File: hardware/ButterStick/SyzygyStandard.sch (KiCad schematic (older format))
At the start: 9 parts, among them J1 SYZYGY-STD, U2 DAC081C081CIMK, U7 TPS73101DBV

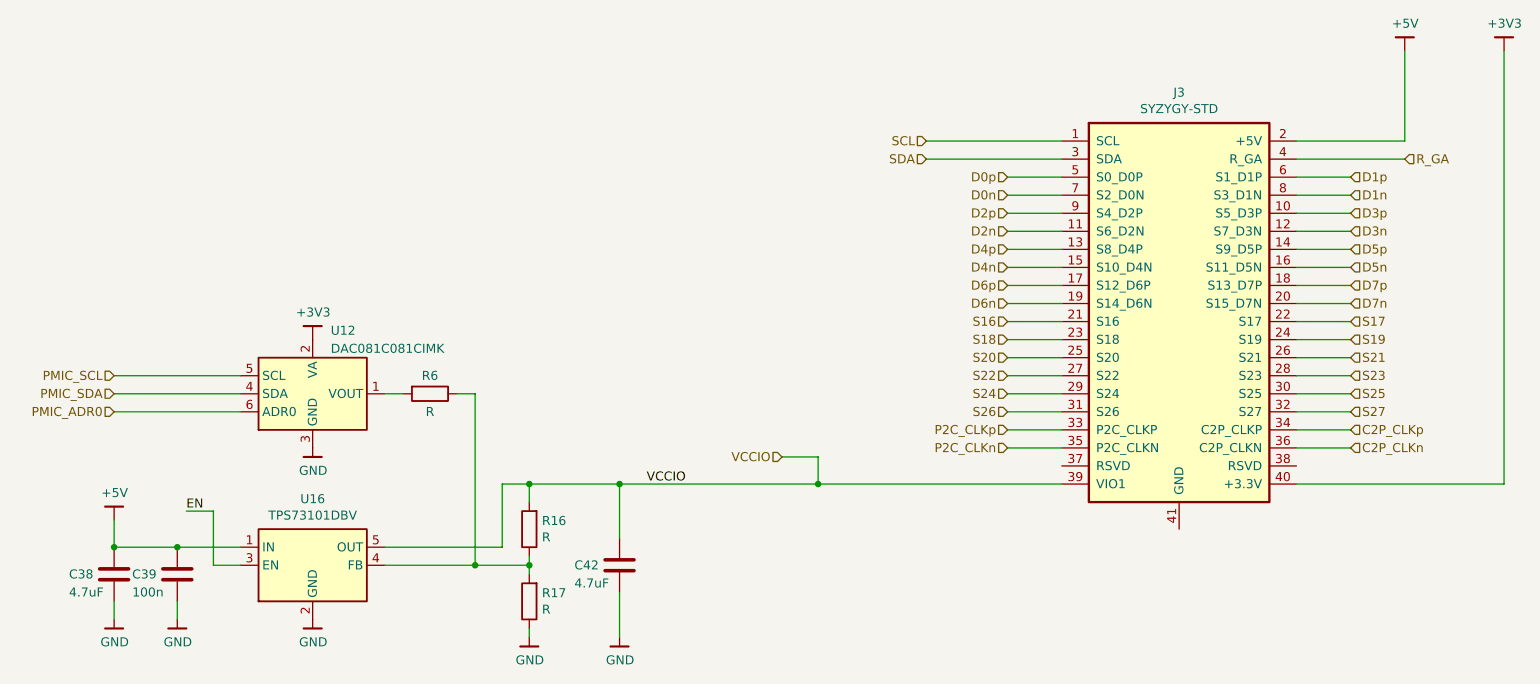
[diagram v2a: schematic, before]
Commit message: Added ESD on SD card signals.
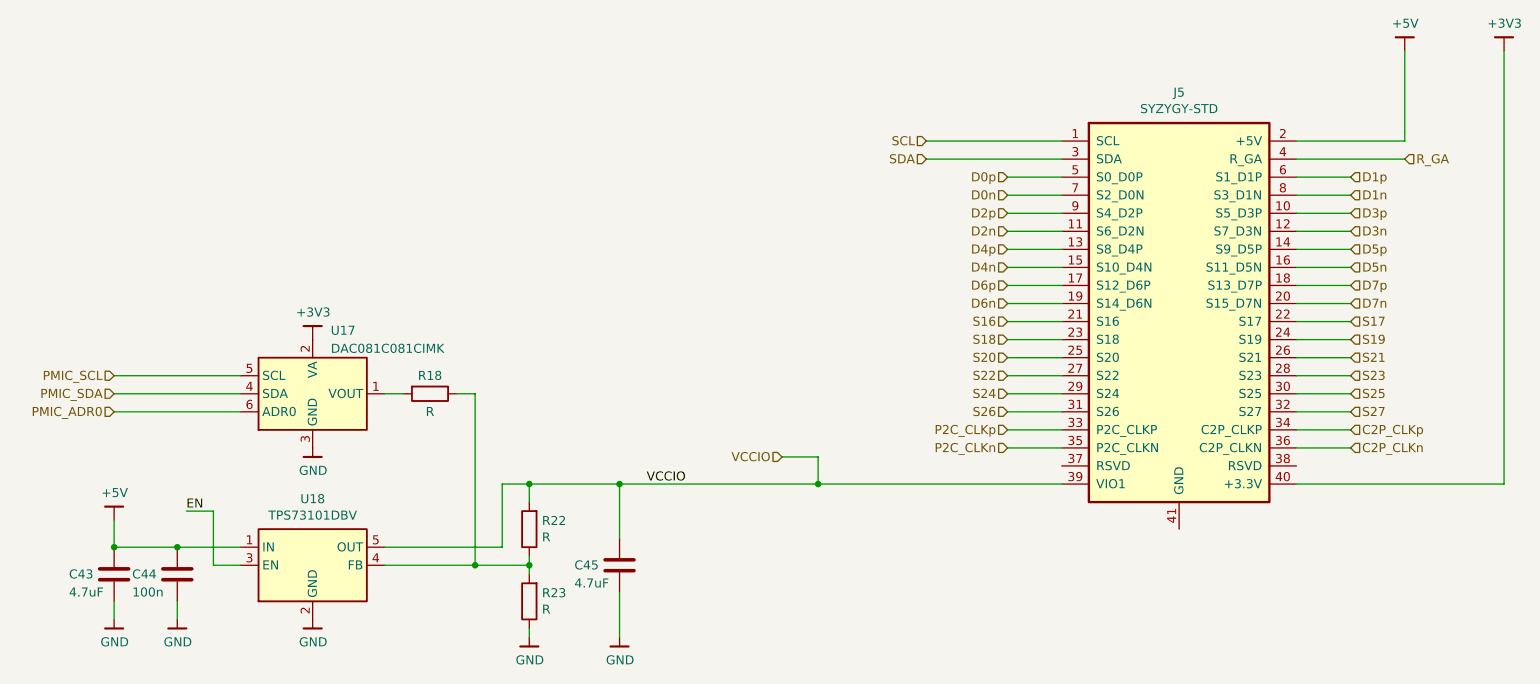
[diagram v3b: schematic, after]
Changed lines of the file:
@@
 $Descr A4 11693 8268
 encoding utf-8
-Sheet 13 14
+Sheet 9 13
 Title ""
 Date ""
@@
 AR Path="/5C80F19D/5C8A3B67/5C813052" Ref="J3"  Part="1"
 AR Path="/5C80F1A0/5C8EBB21/5C813052" Ref="J5"  Part="1"
-F 0 "J3" H 7850 4819 50  0000 C CNN
+F 0 "J5" H 7850 4819 50  0000 C CNN
 F 1 "SYZYGY-STD" H 7850 4728 50  0000 C CNN
 F 2 "gkl_conn:SYZYGY_standard_carrier" H 7850 4700 50  0001 C CNN
@@
 AR Path="/5C80F19D/5C8A3B67/5C939EEE" Ref="U16"  Part="1"
 AR Path="/5C80F1A0/5C8EBB21/5C939EEE" Ref="U18"  Part="1"
-F 0 "U16" H 3050 5567 50  0000 C CNN
+F 0 "U18" H 3050 5567 50  0000 C CNN
 F 1 "TPS73101DBV" H 3050 5476 50  0000 C CNN
 F 2 "Package_TO_SOT_SMD:SOT-23-5" H 3050 5525 50  0001 C CIN
@@
 AR Path="/5C80F19D/5C8A3B67/5C939EF5" Ref="U12"  Part="1"
 AR Path="/5C80F1A0/5C8EBB21/5C939EF5" Ref="U17"  Part="1"
-F 0 "U12" H 3150 4600 50  0000 L CNN
+F 0 "U17" H 3150 4600 50  0000 L CNN
 F 1 "DAC081C081CIMK" H 3150 4500 50  0000 L CNN
 F 2 "Package_TO_SOT_SMD:SOT-23-6" H 3700 4000 50  0001 C CNN
@@
 AR Path="/5C80F19D/5C8A3B67/5C9A2E64" Ref="#PWR0140"  Part="1"
 AR Path="/5C80F1A0/5C8EBB21/5C9A2E64" Ref="#PWR0183"  Part="1"
-F 0 "#PWR0140" H 3050 4300 50  0001 C CNN
+F 0 "#PWR0183" H 3050 4300 50  0001 C CNN
 F 1 "GND" H 3053 4424 50  0000 C CNN
 F 2 "" H 2950 4200 50  0001 C CNN
@@
 AR Path="/5C80F19D/5C8A3B67/5C939F02" Ref="#PWR0173"  Part="1"
 AR Path="/5C80F1A0/5C8EBB21/5C939F02" Ref="#PWR0184"  Part="1"
-F 0 "#PWR0173" H 3050 5250 50  0001 C CNN
+F 0 "#PWR0184" H 3050 5250 50  0001 C CNN
 F 1 "GND" H 3053 5374 50  0000 C CNN
 F 2 "" H 2950 5150 50  0001 C CNN
@@
 AR Path="/5C80F19D/5C8A3B67/5C9A2E66" Ref="#PWR0174"  Part="1"
 AR Path="/5C80F1A0/5C8EBB21/5C9A2E66" Ref="#PWR0185"  Part="1"
-F 0 "#PWR0174" H 3050 3800 50  0001 C CNN
+F 0 "#PWR0185" H 3050 3800 50  0001 C CNN
 F 1 "+3V3" H 3053 4101 50  0000 C CNN
 F 2 "" H 3050 3950 50  0001 C CNN
@@
 AR Path="/5C80F19D/5C8A3B67/5C939F0E" Ref="#PWR0175"  Part="1"
 AR Path="/5C80F1A0/5C8EBB21/5C939F0E" Ref="#PWR0186"  Part="1"
-F 0 "#PWR0175" H 1950 4800 50  0001 C CNN
+F 0 "#PWR0186" H 1950 4800 50  0001 C CNN
 F 1 "+5V" H 1953 5101 50  0000 C CNN
 F 2 "" H 1950 4950 50  0001 C CNN
@@
 AR Path="/5C80F19D/5C8A3B67/5C9A2E68" Ref="C38"  Part="1"
 AR Path="/5C80F1A0/5C8EBB21/5C9A2E68" Ref="C43"  Part="1"
-F 0 "C38" H 1700 5250 50  0000 L CNN
+F 0 "C43" H 1700 5250 50  0000 L CNN
 F 1 "4.7uF" H 1700 5150 50  0000 L CNN
 F 2 "pkl_dipol:C_0603" H 1988 5100 50  0001 C CNN
@@
 AR Path="/5C80F19D/5C8A3B67/5C939F1D" Ref="C39"  Part="1"
 AR Path="/5C80F1A0/5C8EBB21/5C939F1D" Ref="C44"  Part="1"
-F 0 "C39" H 2050 5250 50  0000 L CNN
+F 0 "C44" H 2050 5250 50  0000 L CNN
 F 1 "100n" H 2050 5150 50  0000 L CNN
 F 2 "pkl_dipol:C_0402" H 2338 5100 50  0001 C CNN
@@
 AR Path="/5C80F19D/5C8A3B67/5C9A2E6A" Ref="R6"  Part="1"
 AR Path="/5C80F1A0/5C8EBB21/5C9A2E6A" Ref="R18"  Part="1"
-F 0 "R6" V 3600 4250 50  0000 C CNN
+F 0 "R18" V 3600 4250 50  0000 C CNN
 F 1 "R" V 3800 4250 50  0000 C CNN
 F 2 "pkl_dipol:C_0402" V 3630 4250 50  0001 C CNN
@@
 AR Path="/5C80F19D/5C8A3B67/5C939F38" Ref="R16"  Part="1"
 AR Path="/5C80F1A0/5C8EBB21/5C939F38" Ref="R22"  Part="1"
-F 0 "R16" H 4180 4954 50  0000 R CNN
+F 0 "R22" H 4180 4954 50  0000 R CNN
 F 1 "R" H 4180 5045 50  0000 R CNN
 F 2 "pkl_dipol:C_0402" V 4180 5000 50  0001 C CNN
@@
 AR Path="/5C80F19D/5C8A3B67/5C939F3F" Ref="R17"  Part="1"
 AR Path="/5C80F1A0/5C8EBB21/5C939F3F" Ref="R23"  Part="1"
-F 0 "R17" H 4180 5354 50  0000 R CNN
+F 0 "R23" H 4180 5354 50  0000 R CNN
 F 1 "R" H 4180 5445 50  0000 R CNN
 F 2 "pkl_dipol:C_0402" V 4180 5400 50  0001 C CNN
@@
 AR Path="/5C80F19D/5C8A3B67/5C939F46" Ref="C42"  Part="1"
 AR Path="/5C80F1A0/5C8EBB21/5C939F46" Ref="C45"  Part="1"
-F 0 "C42" H 4500 5200 50  0000 L CNN
+F 0 "C45" H 4500 5200 50  0000 L CNN
 F 1 "4.7uF" H 4500 5100 50  0000 L CNN
 F 2 "pkl_dipol:C_0603" H 4788 5050 50  0001 C CNN
@@
 AR Path="/5C80F19D/5C8A3B67/5C939F4E" Ref="#PWR0176"  Part="1"
 AR Path="/5C80F1A0/5C8EBB21/5C939F4E" Ref="#PWR0187"  Part="1"
-F 0 "#PWR0176" H 4250 5350 50  0001 C CNN
+F 0 "#PWR0187" H 4250 5350 50  0001 C CNN
 F 1 "GND" H 4253 5474 50  0000 C CNN
 F 2 "" H 4150 5250 50  0001 C CNN
@@
 AR Path="/5C80F19D/5C8A3B67/5C9A2E6F" Ref="#PWR0177"  Part="1"
 AR Path="/5C80F1A0/5C8EBB21/5C9A2E6F" Ref="#PWR0188"  Part="1"
-F 0 "#PWR0177" H 4750 5350 50  0001 C CNN
+F 0 "#PWR0188" H 4750 5350 50  0001 C CNN
 F 1 "GND" H 4753 5474 50  0000 C CNN
 F 2 "" H 4650 5250 50  0001 C CNN
@@
 AR Path="/5C80F19D/5C8A3B67/5C939F6F" Ref="#PWR0178"  Part="1"
 AR Path="/5C80F1A0/5C8EBB21/5C939F6F" Ref="#PWR0189"  Part="1"
-F 0 "#PWR0178" H 2300 5250 50  0001 C CNN
+F 0 "#PWR0189" H 2300 5250 50  0001 C CNN
 F 1 "GND" H 2303 5374 50  0000 C CNN
 F 2 "" H 2200 5150 50  0001 C CNN
@@
 AR Path="/5C80F19D/5C8A3B67/5C939F75" Ref="#PWR0179"  Part="1"
 AR Path="/5C80F1A0/5C8EBB21/5C939F75" Ref="#PWR0190"  Part="1"
-F 0 "#PWR0179" H 1950 5250 50  0001 C CNN
+F 0 "#PWR0190" H 1950 5250 50  0001 C CNN
 F 1 "GND" H 1953 5374 50  0000 C CNN
 F 2 "" H 1850 5150 50  0001 C CNN
@@
 AR Path="/5C80F19D/5C8A3B67/5C946418" Ref="#PWR0181"  Part="1"
 AR Path="/5C80F1A0/5C8EBB21/5C946418" Ref="#PWR0191"  Part="1"
-F 0 "#PWR0181" H 9100 2200 50  0001 C CNN
+F 0 "#PWR0191" H 9100 2200 50  0001 C CNN
 F 1 "+5V" H 9103 2501 50  0000 C CNN
 F 2 "" H 9100 2350 50  0001 C CNN
@@
 AR Path="/5C80F19D/5C8A3B67/5C946494" Ref="#PWR0182"  Part="1"
 AR Path="/5C80F1A0/5C8EBB21/5C946494" Ref="#PWR0211"  Part="1"
-F 0 "#PWR0182" H 9650 2200 50  0001 C CNN
+F 0 "#PWR0211" H 9650 2200 50  0001 C CNN
 F 1 "+3V3" H 9653 2501 50  0000 C CNN
 F 2 "" H 9650 2350 50  0001 C CNN

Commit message: Finished initial routing of PCB.. Most parts are finished.
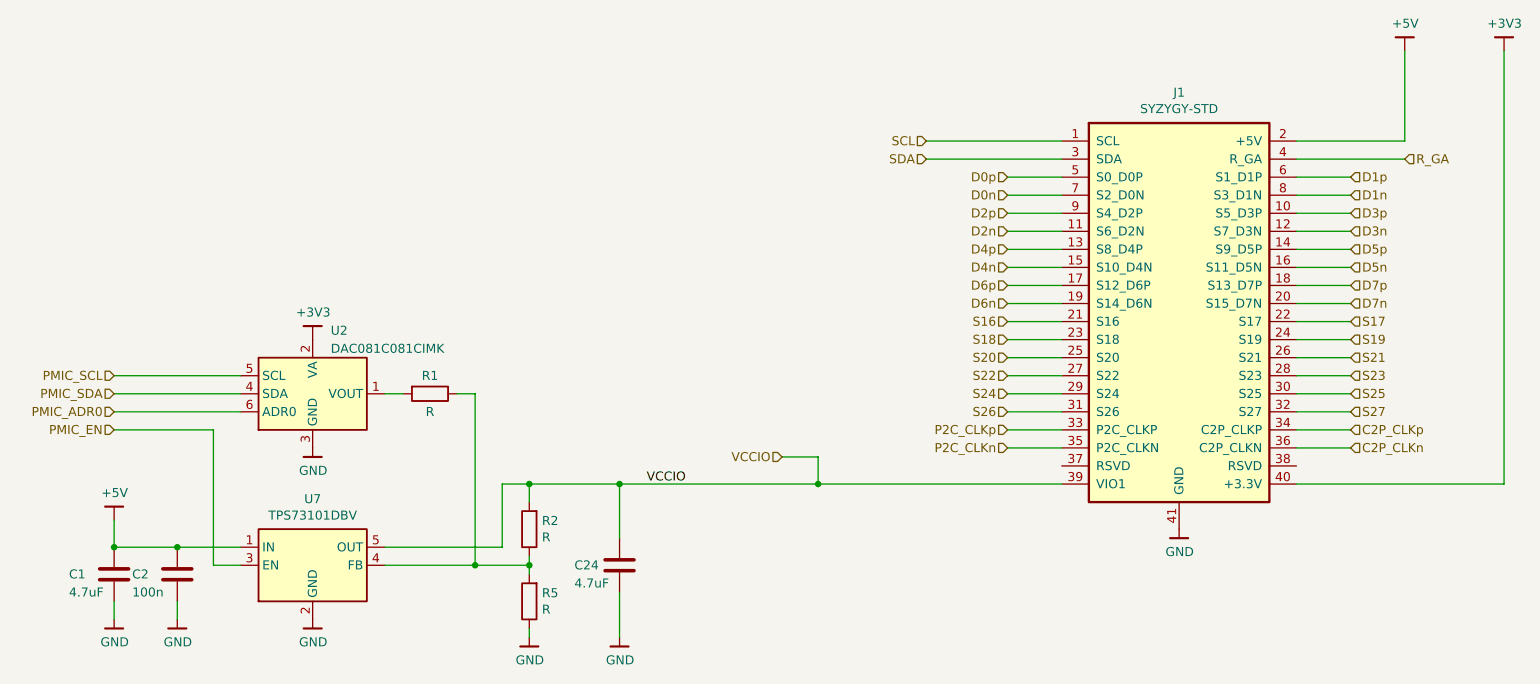
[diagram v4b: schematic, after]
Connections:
- net GND: now also J1.41 (GND)
- net EN renamed PMIC_EN
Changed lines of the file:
@@
 $Descr A4 11693 8268
 encoding utf-8
-Sheet 9 13
+Sheet 8 13
 Title ""
 Date ""
@@
 AR Path="/5C80F19D/5C8A3B67/5C813052" Ref="J3"  Part="1"
 AR Path="/5C80F1A0/5C8EBB21/5C813052" Ref="J5"  Part="1"
-F 0 "J5" H 7850 4819 50  0000 C CNN
+F 0 "J1" H 7850 4819 50  0000 C CNN
 F 1 "SYZYGY-STD" H 7850 4728 50  0000 C CNN
 F 2 "gkl_conn:SYZYGY_standard_carrier" H 7850 4700 50  0001 C CNN
@@
 AR Path="/5C80F19D/5C8A3B67/5C939EEE" Ref="U16"  Part="1"
 AR Path="/5C80F1A0/5C8EBB21/5C939EEE" Ref="U18"  Part="1"
-F 0 "U18" H 3050 5567 50  0000 C CNN
+F 0 "U7" H 3050 5567 50  0000 C CNN
 F 1 "TPS73101DBV" H 3050 5476 50  0000 C CNN
 F 2 "Package_TO_SOT_SMD:SOT-23-5" H 3050 5525 50  0001 C CIN
@@
 AR Path="/5C80F19D/5C8A3B67/5C939EF5" Ref="U12"  Part="1"
 AR Path="/5C80F1A0/5C8EBB21/5C939EF5" Ref="U17"  Part="1"
-F 0 "U17" H 3150 4600 50  0000 L CNN
+F 0 "U2" H 3150 4600 50  0000 L CNN
 F 1 "DAC081C081CIMK" H 3150 4500 50  0000 L CNN
 F 2 "Package_TO_SOT_SMD:SOT-23-6" H 3700 4000 50  0001 C CNN
@@
 AR Path="/5C80F19D/5C8A3B67/5C9A2E68" Ref="C38"  Part="1"
 AR Path="/5C80F1A0/5C8EBB21/5C9A2E68" Ref="C43"  Part="1"
-F 0 "C43" H 1700 5250 50  0000 L CNN
+F 0 "C1" H 1700 5250 50  0000 L CNN
 F 1 "4.7uF" H 1700 5150 50  0000 L CNN
 F 2 "pkl_dipol:C_0603" H 1988 5100 50  0001 C CNN
@@
 AR Path="/5C80F19D/5C8A3B67/5C939F1D" Ref="C39"  Part="1"
 AR Path="/5C80F1A0/5C8EBB21/5C939F1D" Ref="C44"  Part="1"
-F 0 "C44" H 2050 5250 50  0000 L CNN
+F 0 "C2" H 2050 5250 50  0000 L CNN
 F 1 "100n" H 2050 5150 50  0000 L CNN
 F 2 "pkl_dipol:C_0402" H 2338 5100 50  0001 C CNN
@@
 	2650 5200 2500 5200
 Wire Wire Line
-	2500 5200 2500 4900
-Wire Wire Line
-	2500 4900 2350 4900
-Text Label 2350 4900 0    50   ~ 0
-EN
+	2500 5200 2500 4450
 $Comp
 L Device:R R?
@@
 AR Path="/5C80F19D/5C8A3B67/5C9A2E6A" Ref="R6"  Part="1"
 AR Path="/5C80F1A0/5C8EBB21/5C9A2E6A" Ref="R18"  Part="1"
-F 0 "R18" V 3600 4250 50  0000 C CNN
+F 0 "R1" V 3600 4250 50  0000 C CNN
 F 1 "R" V 3800 4250 50  0000 C CNN
 F 2 "pkl_dipol:C_0402" V 3630 4250 50  0001 C CNN
@@
 AR Path="/5C80F19D/5C8A3B67/5C939F38" Ref="R16"  Part="1"
 AR Path="/5C80F1A0/5C8EBB21/5C939F38" Ref="R22"  Part="1"
-F 0 "R22" H 4180 4954 50  0000 R CNN
+F 0 "R2" H 4180 4954 50  0000 R CNN
 F 1 "R" H 4180 5045 50  0000 R CNN
 F 2 "pkl_dipol:C_0402" V 4180 5000 50  0001 C CNN
@@
 AR Path="/5C80F19D/5C8A3B67/5C939F3F" Ref="R17"  Part="1"
 AR Path="/5C80F1A0/5C8EBB21/5C939F3F" Ref="R23"  Part="1"
-F 0 "R23" H 4180 5354 50  0000 R CNN
+F 0 "R5" H 4180 5354 50  0000 R CNN
 F 1 "R" H 4180 5445 50  0000 R CNN
 F 2 "pkl_dipol:C_0402" V 4180 5400 50  0001 C CNN
@@
 AR Path="/5C80F19D/5C8A3B67/5C939F46" Ref="C42"  Part="1"
 AR Path="/5C80F1A0/5C8EBB21/5C939F46" Ref="C45"  Part="1"
-F 0 "C45" H 4500 5200 50  0000 L CNN
+F 0 "C24" H 4500 5200 50  0000 L CNN
 F 1 "4.7uF" H 4500 5100 50  0000 L CNN
 F 2 "pkl_dipol:C_0603" H 4788 5050 50  0001 C CNN
@@
 Wire Wire Line
 	5850 4750 7200 4750
+$Comp
+L gkl_power:GND #PWR?
+U 1 1 5CED2F7B
+P 7850 5000
+AR Path="/5BBD18EA/5CED2F7B" Ref="#PWR?"  Part="1"
+AR Path="/5C80F19A/5C812FEF/5CED2F7B" Ref="#PWR0264"  Part="1"
+AR Path="/5C80F19D/5C8A3B67/5CED2F7B" Ref="#PWR0265"  Part="1"
+AR Path="/5C80F1A0/5C8EBB21/5CED2F7B" Ref="#PWR0266"  Part="1"
+F 0 "#PWR0266" H 7850 4750 50  0001 C CNN
+F 1 "GND" H 7853 4874 50  0000 C CNN
+F 2 "" H 7750 4650 50  0001 C CNN
+F 3 "" H 7850 5000 50  0001 C CNN
+	1    7850 5000
+	1    0    0    -1
+$EndComp
+Text HLabel 1950 4450 0    50   Input ~ 0
+PMIC_EN
+Wire Wire Line
+	1950 4450 2500 4450
 $EndSCHEMATC

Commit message: Update KiCad PCB.
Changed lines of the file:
@@
 AR Path="/5C80F19D/5C8A3B67/5C813052" Ref="J3"  Part="1"
 AR Path="/5C80F1A0/5C8EBB21/5C813052" Ref="J5"  Part="1"
-F 0 "J1" H 7850 4819 50  0000 C CNN
+F 0 "J5" H 7850 4819 50  0000 C CNN
 F 1 "SYZYGY-STD" H 7850 4728 50  0000 C CNN
 F 2 "gkl_conn:SYZYGY_standard_carrier" H 7850 4700 50  0001 C CNN
@@
 AR Path="/5C80F19D/5C8A3B67/5C939EEE" Ref="U16"  Part="1"
 AR Path="/5C80F1A0/5C8EBB21/5C939EEE" Ref="U18"  Part="1"
-F 0 "U7" H 3050 5567 50  0000 C CNN
+F 0 "U18" H 3050 5567 50  0000 C CNN
 F 1 "TPS73101DBV" H 3050 5476 50  0000 C CNN
 F 2 "Package_TO_SOT_SMD:SOT-23-5" H 3050 5525 50  0001 C CIN
@@
 AR Path="/5C80F19D/5C8A3B67/5C939EF5" Ref="U12"  Part="1"
 AR Path="/5C80F1A0/5C8EBB21/5C939EF5" Ref="U17"  Part="1"
-F 0 "U2" H 3150 4600 50  0000 L CNN
+F 0 "U17" H 3150 4600 50  0000 L CNN
 F 1 "DAC081C081CIMK" H 3150 4500 50  0000 L CNN
 F 2 "Package_TO_SOT_SMD:SOT-23-6" H 3700 4000 50  0001 C CNN
@@
 AR Path="/5C80F19D/5C8A3B67/5C9A2E68" Ref="C38"  Part="1"
 AR Path="/5C80F1A0/5C8EBB21/5C9A2E68" Ref="C43"  Part="1"
-F 0 "C1" H 1700 5250 50  0000 L CNN
+F 0 "C43" H 1700 5250 50  0000 L CNN
 F 1 "4.7uF" H 1700 5150 50  0000 L CNN
 F 2 "pkl_dipol:C_0603" H 1988 5100 50  0001 C CNN
@@
 AR Path="/5C80F19D/5C8A3B67/5C939F1D" Ref="C39"  Part="1"
 AR Path="/5C80F1A0/5C8EBB21/5C939F1D" Ref="C44"  Part="1"
-F 0 "C2" H 2050 5250 50  0000 L CNN
+F 0 "C44" H 2050 5250 50  0000 L CNN
 F 1 "100n" H 2050 5150 50  0000 L CNN
 F 2 "pkl_dipol:C_0402" H 2338 5100 50  0001 C CNN
@@
 AR Path="/5C80F19D/5C8A3B67/5C9A2E6A" Ref="R6"  Part="1"
 AR Path="/5C80F1A0/5C8EBB21/5C9A2E6A" Ref="R18"  Part="1"
-F 0 "R1" V 3600 4250 50  0000 C CNN
+F 0 "R18" V 3600 4250 50  0000 C CNN
 F 1 "R" V 3800 4250 50  0000 C CNN
 F 2 "pkl_dipol:C_0402" V 3630 4250 50  0001 C CNN
@@
 AR Path="/5C80F19D/5C8A3B67/5C939F38" Ref="R16"  Part="1"
 AR Path="/5C80F1A0/5C8EBB21/5C939F38" Ref="R22"  Part="1"
-F 0 "R2" H 4180 4954 50  0000 R CNN
+F 0 "R22" H 4180 4954 50  0000 R CNN
 F 1 "R" H 4180 5045 50  0000 R CNN
 F 2 "pkl_dipol:C_0402" V 4180 5000 50  0001 C CNN
@@
 AR Path="/5C80F19D/5C8A3B67/5C939F3F" Ref="R17"  Part="1"
 AR Path="/5C80F1A0/5C8EBB21/5C939F3F" Ref="R23"  Part="1"
-F 0 "R5" H 4180 5354 50  0000 R CNN
+F 0 "R23" H 4180 5354 50  0000 R CNN
 F 1 "R" H 4180 5445 50  0000 R CNN
 F 2 "pkl_dipol:C_0402" V 4180 5400 50  0001 C CNN
@@
 AR Path="/5C80F19D/5C8A3B67/5C939F46" Ref="C42"  Part="1"
 AR Path="/5C80F1A0/5C8EBB21/5C939F46" Ref="C45"  Part="1"
-F 0 "C24" H 4500 5200 50  0000 L CNN
+F 0 "C45" H 4500 5200 50  0000 L CNN
 F 1 "4.7uF" H 4500 5100 50  0000 L CNN
 F 2 "pkl_dipol:C_0603" H 4788 5050 50  0001 C CNN
